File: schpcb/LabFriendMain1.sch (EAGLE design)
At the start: 299 parts, among them IC1 TPS62560, IC10 TPS62560, IC11 TPS62560, IC12 TPS62560, IC14 TPS72301, IC18 LM358D, IC19 LM358D, IC2 25px80, IC20 PCM3010, IC21 TS922, IC23 TS922, IC24 4052D, IC25 ADS1112, IC26 MT41J128M8, IC3 SI8462, IC4 FT232H, IC5 ADC08200, IC6 ADC08200, IC8 93LC56SM, IC9 74LVC8T245, Q1 12MHz, U2 6SLX9FTG256, X1 MINI-USB-32005-201

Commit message: current state
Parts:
- added C100, C102: 2n2, passive:CAPC0603
- added C101, C114, C98, C99: 330pF, passive:CAPC0603
- added C103, C113: 47uF, passive:CAPC1206
- added C115, C116, C145, C146, C147, C193, C197, C198, C96, C97: 100nF, passive:CAPC0402
- added C148, C150: (no value), passive:CAPC0402
- added C149: 100pF, teg2:C0603
- added C151, C152: 47pF, teg2:C0603
- added C153, C154: 100n, teg2:C0603
- added C155, C156, C160: 100nF, teg2:C0603
- added C157, C158, C159, C161: 100µF, rcl:CPOL-EUCT6032
- added C162, C173, C178, C181, C188, C189, C191, C196, C199: 1uF, passive:CAPC0603
- added C163, C174: 22pF, passive:CAPC0603
- added C164: 100uF, passive:CAPC0402
- added C165, C171, C177, C179, C180, C182, C183, C184, C185, C186, C187, C192, C194, C200: 10uF, passive:CAPC0603
- added C166: 470nF, passive:CAPC1206
- added C167: 470nF, passive:CAPC0402
- added C168, C169, C170, C175, C176: 10µF, passive:CAPC0603
- added C172, C190, C195: 10nF, passive:CAPC0603
- added D1, D2, D3, D4, D5, D6: SK14, diode:DIODE-DO214AC
- added IC13: AK4621, data-converters:AK4621
- added IC15: LME49721, linear:LM358D
- added IC16: NE5532, linear:LM358D
- added IC17: OPA2134, linear:LM358D
- added IC22: 4052D, 40xx:4052D
- added IC27: 74HCT132D, 74xx-eu:74HCT132D
- added IC28: TPS72301, seabed:TPS72301
- added IC29: (no value), seabed:TPS73001
- added IC30: LM8272, linear:LMV358MM
- added IC31: LMV358MM, linear:LMV358MM
- added L11: (no value), passive:INUDCTOR0603
- added Q2, Q3: FDN335N, transistor-small-signal:BSS123
- added R132, R133, R134: 1k5, passive:RESR0603
- added R135, R136, R137, R138: 3k, passive:RESR0603
- added R139, R140, R141, R142: 22R, teg2:R0603
- added R143, R144: 10k, passive:RESR0603
- added R145, R147, R148, R149, R181, R182, R189, R190, R191, R194, R196, R200, R58, R74: 4k7, passive:RESR0603
- added R146, R150: 220k, passive:RESR0603
- added R151: 4k7, teg2:R0603
- added R152: 100R, teg2:R0603
- added R153, R163, R164, R166, R167, R175, R176: (no value), passive:RESR0603
- added R154: 1M, passive:RESR0603
- added R155, R187, R188: 100k, passive:RESR0603
- added R156: 1k, passive:RESR0603
- added R157, R158: 10k, teg2:R0603
- added R159, R160: 1.54k, teg2:R0603
- added R161, R162: 150, teg2:R0603
- added R165, R168, R172, R173, R174, R177, R178, R179, R180, R183, R184, R185, R186, R192, R193: 0R1, passive:RESR0603
- added R169: 1M, passive:RESR0402
- added R170, R171: 820k, passive:RESR0603
- added R195: 1k3, passive:RESR0603
- added R197: 5k1, passive:RESR0603
- added R198: 68k, passive:RESR0603
- added R199: 15k, passive:RESR0603
- added R56, R57: 200, passive:RESR0603
- added T1: EFD15DCDCPM5P33EFD15, transformers:EFD15DCDCPM5P33EFD15
- C1, C2, C3, C78, C79, C80, C82, C88, C92, C93: device teg2:C0603 -> passive:CAPC0603
- C104, C105, C112: device teg2:C0603 -> passive:CAPC0402
- C106, C107, C108, C109, C110, C111, C118, C125, C13, C134, C137, C138, C14, C140, C141, C28, C32, C33, C58, C60, C61, C62, C63, C64, C65, C67, C68, C69, C76, C77: device rcl:C-EUC0402 -> passive:CAPC0402
- C11: device rcl:C-EUC1206 -> passive:CAPC1206
- C117, C126: value 10uF -> 100nF; device rcl:C-EUC0603K -> passive:CAPC0402
- C119, C29, C30, C31, C36, C37, C39, C40, C41, C42, C43, C44, C45, C46, C47, C48, C49, C50, C52, C53, C54, C55, C56, C74: device rcl:C-EUC0603K -> passive:CAPC0603
- C12, C57, C59, C66, C70: device rcl:C-EUC0603 -> passive:CAPC0603
- C120, C73: value 100nF -> 10uF; device rcl:C-EUC0402 -> passive:CAPC0603
- C121, C123: value 10uF -> 330pF; device rcl:C-EUC0603K -> passive:CAPC0603
- C122, C124: value 100nF -> 330pF; device rcl:C-EUC0402 -> passive:CAPC0603
- C127: value 10uF -> 10nF; device rcl:C-EUC0603K -> passive:CAPC0603
- C128: value 200pF -> 330pF; device rcl:C-EUC0603K -> passive:CAPC0603
- C129, C130, C131, C132, C133: value 200pF -> 47uF; device rcl:C-EUC0603K -> passive:CAPC1206
- C135, C136: value 10uF -> 47uF; device rcl:C-EUC0603K -> passive:CAPC1206; VOLTAGE (none) -> 10V
- C21, C23, C35: value 4u7 -> 100uF; device rcl:C-EUC0603K -> passive:CAPC1206
- C22, C25: value 4u7 -> 470nF; device rcl:C-EUC0603K -> passive:CAPC0402
- C24: value 4u7 -> 10uF; device rcl:C-EUC0603K -> passive:CAPC0603
- C26, C38: device rcl:C-EUC0603K -> passive:CAPC0402
- C34: value 470nF -> 10uF; device rcl:C-EUC0402 -> passive:CAPC0603
- C71: value 10uF -> 100uF; device rcl:C-EUC0603 -> passive:CAPC1206
- C72: value 100nF -> 470nF; device rcl:C-EUC0402 -> passive:CAPC0402
- C81: value 33pF -> 10uF; device teg2:C0603 -> passive:CAPC0603
- C83, C87: value 10µF -> 10nF; device teg2:C0603 -> passive:CAPC0603
- C84: value 33pF -> 1uF; device teg2:C0603 -> passive:CAPC0603
- C85: value 10µF -> 22pF; device teg2:C0603 -> passive:CAPC0603
- C86: value 10µF -> 10uF; device teg2:C0603 -> passive:CAPC0603
- C91, C95: device passive:CAPC0402 -> passive:CAPC0603
- IC11, IC12: value TPS62560 -> (none); device seabed:TPS62560 -> seabed:TPS73001
- IC18: value LM358D -> LM8272; device linear:LM358D -> linear:LMV358MM
- IC19: value LM358D -> LMV358MM; device linear:LM358D -> linear:LMV358MM
- IC20: value PCM3010 -> ISL54405IRTZ; device parts2004:PCM3010 -> switch_mux:ISL54405IRTZ
- IC21: value TS922 -> NE5532
- IC23: value TS922 -> LME49721
- IC24: value 4052D -> 74HC00D; device 40xx:4052D -> 74xx-eu:74HC00D
- L10, L8, L9: value 4.7uH -> (none); device rcl:L-USL3216C -> passive:INUDCTOR0603
- R10, R100, R101, R102, R103, R11, R12, R22, R23, R24, R25, R26, R27, R28, R29, R30, R31, R32, R33, R34, R35, R36, R37, R4, R5, R6, R79, R8, R88, R89, R9, R97, R98, R99: device teg2:R0603 -> passive:RESR0402
- R105, R94: value 47R -> 200; device teg2:R0603 -> passive:RESR0603
- R106: value 47R -> 1k5; device teg2:R0603 -> passive:RESR0603
- R107, R112, R14, R15, R16, R17, R18, R19, R20, R21, R38, R39, R40, R41, R42, R43, R44, R45, R46, R47, R52, R53, R65, R66, R75, R76, R77, R78, R93: device teg2:R0603 -> passive:RESR0603
- R48, R50: value 820k -> 0R1; device teg2:R0603 -> passive:RESR0603
- R49, R51: value 180k -> 0R1; device teg2:R0603 -> passive:RESR0603
- R54, R55: value RESR0603 -> (none)
- R61, R63: value 51k -> 68k; device teg2:R0603 -> passive:RESR0603
- R62, R64: value 22k -> 15k; device teg2:R0603 -> passive:RESR0603
- R83, R91: value 10M -> 4k7; device teg2:R0603 -> passive:RESR0603
- R84, R85: value 6k8 -> 4k7; device teg2:R0603 -> passive:RESR0603
- R86, R87: value 47R -> 600R
- R92: value 47R -> 4k7; device teg2:R0603 -> passive:RESR0603
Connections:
- removed net +5V/1: C3.2, C80.2, C83.2, C86.2, IC1.EN, IC1.VIN, IC10.EN, IC10.VIN, IC11.EN, IC11.VIN, IC12.EN, IC12.VIN
- removed net -2V2: C105.2, C137.1, C141.2, IC18P.V-, IC23P.V-, IC24P.VEE
- removed net ASEL1: IC24A.B
- removed net HPADSPICS: IC3.B5, U2B2.IO_L31P_GCLK31_D14_2
- new net +3.6VBR: C162.2, C3.2, C80.2, C84.2, IC1.EN, IC1.VIN, IC10.EN, IC10.VIN, IC11.EN, IC11.IN, IC12.EN, IC12.IN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
- new net +3.6VI: C94.2, IC7.EN, IC7.IN, R179.P$1
- new net +5.5V: C156.1, C157.+, D1.C, D2.C, R178.P$1
- new net +5.5VI: C173.2, IC29.EN, IC29.IN, R178.P$2
- new net -2.5VI: C93.1, IC14.OUT, R174.P$1, R52.P$2
- new net -2V5: C176.1, C198.2, R174.P$2
- new net -5.5V: C155.2, C158.-, D3.A, D4.A, R172.P$1
- new net 1V2REFAD0: C111.1, IC5.VRB, L10.2
- new net 1V2REFAD1: C108.1, IC6.VRB, L9.2
- new net 2V8REFAD0: C109.1, IC5.VRT, L11.2
- new net 2V8REFAD1: C106.1, IC6.VRT, L8.2
- new net AUADCINL: C132.1, IC17B.-IN, IC17B.OUT, R149.P$2
- new net AUADCINR: C130.1, IC17A.-IN, IC17A.OUT, R147.P$2
- new net AUBIAS: C133.2, C134.2, IC15A.-IN, IC15B.+IN, IC23A.+IN, IC23B.+IN, R143.P$1, R144.P$2
- new net AUPDN: IC13.PDN
- new net AU_CCLK: IC13.CCLK/CKS1
- new net AU_CDTI: IC13.CDTI/CKS0
- new net AU_CSN: IC13.CSN/DIF
- new net AU_OVFL: IC13.OVFL/DZFL
- new net AU_OVFR: IC13.OVFR/DZFR
- new net AVREFM: C192.1, R192.P$2
- new net CMPMEAS_+: IC20.L2, R153.P$1, R154.P$1, R155.P$1, R156.P$1, SV4.1
- new net CMPMEAS_-: IC20.R2, IC22A.Y
- new net CMPMEAS_A: IC22A.A
- new net CMPMEAS_B: IC22A.B
- new net CMPMEAS_EN: IC22A.INH
- new net CMPMEAS_O: IC22A.X, R152.P$2
- new net EXVOI: IC19B.OUT, R185.P$1, R75.P$1
- new net LAD13OO: U2B2.IO_L13N_D10_2
- new net LADVREF: C167.1, R169.P$2, U2B2.IO_L16N_VREF_2, U2B2.IO_L48N_RDWR_B_VREF_2
- new net LAVIOI: C188.2, IC19A.OUT, R186.P$1, R66.P$1
- new net N$111: C101.1, IC21A.-IN, R94.P$2
- new net N$125: C121.1, IC23B.-IN, R106.P$1, R135.P$2
- new net N$152: C122.1, IC15A.+IN, R134.P$1, R137.P$2
- new net N$154: C123.1, IC15B.-IN, R133.P$1, R136.P$2
- new net N$156: C124.1, IC23A.-IN, R132.P$1, R138.P$2
- new net N$158: C127.2, IC13.AINL+, R140.P$1
- new net N$160: C127.1, IC13.AINL-, R139.P$2
- new net N$161: C128.1, IC13.AINR-, R142.P$2
- new net N$166: C128.2, IC13.AINR+, R141.P$1
- new net N$167: C129.2, R135.P$1
- new net N$168: C130.2, R138.P$1
- new net N$169: C131.2, R136.P$1
- new net N$170: C132.2, R137.P$1
- new net N$171: C131.1, IC16B.OUT, R148.P$1
- new net N$172: IC17B.+IN, IC20.R, R150.P$2
- new net N$173: IC17A.+IN, IC20.L, R146.P$2
- new net N$174: C146.2, IC20.CAP_SS
- new net N$175: C129.1, IC16A.OUT, R145.P$1
- new net N$176: IC16A.-IN, R145.P$2, R147.P$1
- new net N$177: IC16B.-IN, R148.P$2, R149.P$1
- new net N$178: IC20.R1, R151.P$1
- new net N$179: IC22A.X0, IC22A.Y0, R153.P$2
- new net N$180: IC22A.X1, IC22A.Y1, R154.P$2
- new net N$181: IC22A.X2, IC22A.Y2, R155.P$2
- new net N$182: IC22A.X3, IC22A.Y3, R156.P$2
- new net N$183: C148.2, C150.1, IC22P.GND
- new net N$184: IC27A.I0, IC27A.I1, R157.P$1
- new net N$185: IC24B.I0, IC24B.I1, IC27A.O
- new net N$186: C149.1, R157.P$2, R158.P$1
- new net N$187: C149.2, IC24A.I0, IC24A.I1, IC24B.O
- new net N$188: IC24A.O, IC27B.I0, IC27B.I1, IC27D.I0, R158.P$2, R160.P$1
- new net N$189: C151.2, IC27D.I1, R160.P$2
- new net N$190: IC27B.O, IC27C.I0, R159.P$1
- new net N$191: C152.2, IC27C.I1, R159.P$2
- new net N$192: IC24C.I0, IC24C.I1, IC27C.O
- new net N$193: IC24D.I0, IC24D.I1, IC27D.O
- new net N$194: IC24D.O, R161.P$1
- new net N$195: IC24C.O, R162.P$1
- new net N$196: Q3.G, R162.P$2
- new net N$197: D2.A, D3.C, T1.S1P
- new net N$198: D1.A, D4.C, T1.S1N
- new net N$199: Q2.D, T1.P1P
- new net N$200: Q2.G, R161.P$2
- new net N$201: Q3.D, T1.P1N
- new net N$202: D5.A, T1.S2P
- new net N$203: D6.A, T1.S2N
- new net N$204: R195.P$2, R197.P$1
- new net N$205: R43.P$1, U2B0.IO_L33P_0
- new net N$206: C81.2, C85.2, IC11.OUT, R163.P$2, R165.P$1
- new net N$207: C85.1, IC11.FB, R163.P$1, R164.P$2
- new net N$208: C163.2, C86.2, IC12.OUT, R166.P$2, R168.P$1
- new net N$209: C163.1, IC12.FB, R166.P$1, R167.P$2
- new net N$210: R169.P$1, U2B2.IO_L64N_D9_2
- new net N$211: C169.1, IC28.OUT, R170.P$2, R173.P$1
- new net N$212: IC28.FB, R170.P$1, R171.P$2
- new net N$213: C190.1, IC30A.OUT, R189.P$1, R192.P$1
- new net N$214: C172.2, IC29.NR
- new net N$215: C171.2, C174.2, IC29.OUT, R175.P$2, R177.P$1
- new net N$216: C174.1, IC29.FB, R175.P$1, R176.P$2
- new net N$217: C190.2, IC30A.-IN, R189.P$2
- new net N$218: C195.1, IC30B.OUT, R191.P$2, R193.P$1, R194.P$1
- new net N$219: C195.2, IC30B.-IN, R194.P$2
- new net N$220: C196.1, IC30B.+IN, R196.P$1, R197.P$2
- new net N$221: C199.1, IC31B.-IN, R198.P$2, R199.P$1
- new net N$223: C200.1, R199.P$2, R200.P$1
- new net N$23: C191.1, IC30A.+IN, R190.P$2, R191.P$1
- new net N$83: C135.2, R58.P$1
- new net N$88: C136.2, R74.P$1
- new net OFFSETCH0I: C178.1, IC18A.OUT, R183.P$1, R61.P$1
- new net OFFSETCH1I: C181.2, IC18B.OUT, R184.P$1, R63.P$1
- new net PWMEXVO: R188.P$2
- new net PWMLA: R200.P$2
- new net PWMLAVIO: R187.P$2
- new net PWMOFFS0: R181.P$2
- new net PWMOFFS1: R182.P$2
- net +3.6V: now also C160.1, C161.+, D5.C, D6.C, R179.P$2, R48.P$1; no longer C94.2, IC7.EN, IC7.IN
- net +3V3: now also C116.1, C117.1, C147.2, C164.2, C165.2, C166.2, IC13.DVDD, IC13.TVDD, R165.P$2, U2B0.IO_L1N_VREF_0, U2B0.IO_L2P_0, U2B0.IO_L3N_0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; no longer C125.1, C21.1, C81.2, IC20.DEMP0, IC20.FMT0, IC20.FMT1, IC20.PDOWN/, L8.2, R48.P$2
- net +5V: now also C104.2, C115.2, C119.2, C125.1, C126.1, C138.1, C141.1, C145.1, C148.1, C170.2, C96.1, IC13.AVDD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; no longer C123.1, C124.1, C134.1, C140.1, IC20.VCC1, IC20.VCC2, IC24P.VCC
- net +UB: now also C153.2, C154.2, C159.+, IC24P.VCC, IC27P.VCC, R51.P$2, T1.P1M; no longer C74.1, L6.1
- net -5V: now also C105.2, C137.1, C140.1, C150.2, C175.1, C97.1, IC16P.V-, IC17P.V-, IC18P.V-, IC21P.V-, IC22P.VEE, R173.P$2; no longer C93.1, IC14.OUT, R52.P$2
- net 1V2REF: now also C194.1, IC31B.+IN, L10.1, L9.1, R193.P$2; no longer C108.1, C111.1, IC24A.X2, IC24A.Y2, IC5.VRB, IC6.VRB
- net 2V8REF: now also C177.2, C193.2, IC30P.V+, L11.1, L8.1, R180.P$1, R190.P$1, R195.P$1; no longer C106.1, C109.1, IC5.VRT, IC6.VRT
- net 3V3A: now also C197.2, R168.P$2; no longer C104.2, C138.2, C87.2, IC18P.V+, IC23P.V+, L10.2
- net ADA0: now also U2B1.IO_L34N_A12_M1BA2_1; no longer U2B1.IO_L32N_A16_M1A9_1
- net ADA1: now also U2B1.IO_L34P_A13_M1WE_1; no longer U2B1.IO_L32P_A17_M1A8_1
- net ADA4: now also U2B1.IO_L33N_A14_M1A4_1; no longer U2B1.IO_L30N_A20_M1A11_1
- net ADA5: now also U2B1.IO_L33P_A15_M1A10_1; no longer U2B1.IO_L30P_A21_M1RESET_1
- net ADAC: now also U2B1.IO_L35P_A11_M1A7_1; no longer U2B1.IO_L33N_A14_M1A4_1
- net ADAP: now also U2B1.IO_L35N_A10_M1A2_1; no longer U2B1.IO_L33P_A15_M1A10_1
- net ADB0: now also U2B1.IO_L41N_GCLK8_M1CASN_1; no longer U2B1.IO_L38P_A5_M1CLK_1
- net ADB1: now also U2B1.IO_L44N_A2_M1DQ7_1; no longer U2B1.IO_L37N_A6_M1A1_1
- net ADB2: now also U2B1.IO_L44P_A3_M1DQ6_1; no longer U2B1.IO_L37P_A7_M1A0_1
- net ADB3: now also U2B1.IO_L43N_GCLK4_M1DQ5_1; no longer U2B1.IO_L36N_A8_M1BA1_1
- net ADB4: now also U2B1.IO_L37N_A6_M1A1_1; no longer U2B1.IO_L36P_A9_M1BA0_1
- net ADB5: now also U2B1.IO_L37P_A7_M1A0_1; no longer U2B1.IO_L35N_A10_M1A2_1
- net ADB6: now also U2B1.IO_L36N_A8_M1BA1_1; no longer U2B1.IO_L35P_A11_M1A7_1
- net ADB7: now also U2B1.IO_L32N_A16_M1A9_1; no longer U2B1.IO_L34N_A12_M1BA2_1
- net ADBC: now also U2B1.IO_L47N_LDC_M1DQ1_1; no longer U2B1.IO_L34P_A13_M1WE_1
- net AINL: no longer R92.P$2
- net AINR: now also R151.P$2; no longer R106.P$2, R93.P$2
- net ASEL0: no longer IC24A.A
- net EXVO: now also C184.1, R185.P$2; no longer IC19B.OUT, R75.P$1
- net GND: now also C114.1, C115.1, C116.2, C118.1, C119.1, C120.1, C126.2, C133.1, C134.1, C138.2, C141.2, C145.2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; no longer C118.2, C119.2, C120.2, C121.2, C122.2, C123.2, C124.2, C128.2, C129.2, C130.2, C131.2, C132.2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
- net GNDIO: now also C151.1, C152.1, C153.1, C154.1, C159.-, IC24P.GND, IC27P.GND, Q2.S, Q3.S
- net I2SBCK: now also IC13.BICK; no longer IC20.BCK, U2B2.IO_L64P_D8_2
- net I2SDATAIN: now also IC13.SDTI; no longer IC20.DIN
- net I2SLRCK: now also IC13.LRCK; no longer IC20.LRCK, U2B2.IO_L64N_D9_2
- net I2SSCLK: now also IC13.MCLK; no longer IC20.SCKI
- net LAD0: now also U2B2.IO_L23N_2
- net LAD1: now also U2B2.IO_L31P_GCLK31_D14_2
- net LAD10: now also U2B2.IO_L47P_2; no longer U2B1.IO_L39P_M1A3_1
- net LAD11: now also U2B2.IO_L29N_GCLK2_2; no longer U2B1.IO_L38N_A4_M1CLKN_1
- net LAD13: now also U2B2.IO_L14N_D12_2; no longer U2B2.IO_L13N_D10_2
- net LAD2: now also U2B2.IO_L30N_GCLK0_USERCCLK_2
- net LAD3: now also U2B2.IO_L32N_GCLK28_2
- net LAD4: now also U2B2.IO_L32P_GCLK29_2
- net LAD5: now also U2B2.IO_L47N_2; no longer U2B1.IO_L41N_GCLK8_M1CASN_1
- net LAD6: now also U2B2.IO_L48P_D7_2; no longer U2B1.IO_L41P_GCLK9_IRDY1_M1RASN_1
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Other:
- note removed: "120k"
- note removed: "3.15V"
- note removed: "3.1V"
- note removed: "510k"
- note removed: "750k"
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
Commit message: Pre release checkin
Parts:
- added C201, C202, C203: 10nF, passive:CAPC0402
- added C204, C206, C207, C208, C209, C210, C218, C219, C220, C221, C225, C226, C227, C231, C232, C233, C234, C235, C243, C244, C245, C246, C250, C251, C252, C255, C256: 100nF, passive:CAPC0402
- added C205, C230: 10uF, passive:CAPC0603
- added C211, C236: 100nF, passive:CAPC0603
- added C212, C214, C217, C222, C223, C237, C239, C242, C247, C248: 12pF, passive:CAPC0603
- added C213, C216, C238, C241: 6/30, rcl:C-TRIMMTZBX4
- added C215, C240: 220pF, passive:CAPC0603
- added C224, C249: 100uF, passive:CAPC1206
- added C228, C229, C253, C254: 1pF, passive:CAPC0603
- added IC32: ADS1118IDGSR, data-converters:ADS1118IDGSR
- added IC33, IC38: ADA4853-3RU, teg4:ADA4853-3RU
- added IC34, IC35, IC39, IC40: 4052D, 40xx:4052D
- added IC36, IC41: OPA2354, linear:AD8682RM
- added IC37, IC42, IC44: 74HC595D, 74xx-eu:74HC595D
- added IC43: LM321MF, linear:LM321MF
- added K1, K2, K3, K4: G6K-2F-Y, relay:G6K-2F-Y
- added L12, L14: 1uH, rcl:L-EUL3216C
- added R201: NC, passive:RESR0402
- added R202: 91k, passive:RESR0603
- added R203, R218, R219, R220, R254, R255, R256: 10k, passive:RESR0603
- added R204, R205: 27k, passive:RESR0603
- added R206, R207: 22k, passive:RESR0603
- added R208, R244: 200R, passive:RESR0603
- added R209, R245: 30R, passive:RESR0603
- added R210, R246: 20R, passive:RESR0603
- added R211, R214, R217, R237, R239, R247, R250, R253, R273, R275, R278, R279: 22R, passive:RESR0603
- added R212, R215, R216, R229, R230, R238, R248, R251, R252, R265, R266, R274, R300: 300R, passive:RESR0603
- added R213, R249, R277: 100R, passive:RESR0603
- added R221, R222, R257, R258: 30k, passive:RESR0603
- added R223, R224, R259, R260: 470k, passive:RESR0603
- added R225, R261: 51k, passive:RESR0603
- added R226, R262: 39k, passive:RESR0603
- added R227, R263: 910k, passive:RESR0603
- added R228, R264: 1k, passive:RESR0603
- added R231, R267: 7R5, passive:RESR0603
- added R232, R233, R234, R235, R236, R268, R269, R270, R271, R272: 10R, passive:RESR0603
- added R240, R276: 1R, passive:RESR0603
- added R241: 100R, passive:RESR0402
- added R242, R243: 47R, passive:RESR0603
- added R280: 1k, passive:RESR0402
- added R281: 2k2, passive:RESR0402
- added R282: 50R, passive:RESR0603
- added R283, R285, R292, R293, R294, R295, R296, R297, R298: 1k6, passive:RESR0603
- added R284, R286, R287, R288, R289, R290, R291: 820R, passive:RESR0603
- added R299: 39R, passive:RESR0603
- added SV5: 3x1 Pinheader, con-lstb:MA03-1
- added T10, T11, T14, T16, T2, T3, T4, T8: BC850, transistor:BC850
- added T12, T13, T15, T17, T5, T6, T7, T9: BC856ASMD, transistor-pnp:BC856ASMD
- added X2, X3: 31-5431-10RFX, connectors:227161-8
- C10, C139, C142, C143, C144, C15, C16, C17, C18, C20, C8, C9: device rcl:C-EUC0402 -> passive:CAPC0402
- C100, C101, C102, C114, C121, C122, C123, C124, C127, C98, C99: TYPE (none) -> NP0/C0G
- C12, C43, C44, C46, C48, C74: value 4.7uF -> 10uF
- C128: value 330pF -> 10nF; TYPE (none) -> NP0/C0G
- C129, C130, C131, C132, C133: VOLTAGE (none) -> 10V
- C148, C150: value (none) -> 100nF
- C149, C151, C152: device teg2:C0603 -> passive:CAPC0603
- C153, C154: value 100n -> 100nF; device teg2:C0603 -> passive:CAPC0402
- C155, C156, C160: device teg2:C0603 -> passive:CAPC0402
- C157, C158, C159, C161: value 100µF -> 100uF
- C163, C174, C85, C95: value 22pF -> 15pF
- C164: value 100uF -> 470nF
- C166: value 470nF -> 100uF
- C168, C169, C170, C175, C176, C2, C3, C79, C80, C82, C88, C92, C93: value 10µF -> 10uF
- C172, C190, C195, C36, C37, C39, C40, C41, C42, C45, C47, C49, C50, C52, C53, C54, C83, C87, C91: device passive:CAPC0603 -> passive:CAPC0402
- C51: device rcl:C-EUC0603K -> passive:CAPC0402
- IC1, IC10: value TPS62560 -> TPS62240DDC
- IC11, IC12, IC29, IC7: value (none) -> TPS73001DBVR
- IC22: value 4052D -> 74HC4052D
- IC25: value ADS1112 -> INA331IDGK; device teg4:ADS1112 -> amplifiers-and-linear:INA331IDGK
- L10, L11, L8, L9: value (none) -> 220nH
- L4, L5: device rcl:L-EUL3216C -> passive:INUDCTOR0603
- R1, R2: value 100 -> 100R; device teg2:R0603 -> passive:RESR0402
- R100, R101, R102, R103, R79, R97, R98, R99: value 47 -> 47R
- R104, R139, R140, R141, R142, R151, R157, R158, R59: device teg2:R0603 -> passive:RESR0603
- R105, R56, R57, R94: value 200 -> 200R
- R107, R46, R47: value 360 -> 360k
- R108, R109, R110, R111: value 6k8 -> 4k7; device teg2:R0603 -> passive:RESR0402
- R112: value 360 -> 240k
- R116, R117, R118, R119, R120, R121, R122, R123: value 100 -> 100R
- R146, R150: value 220k -> 1M
- R152, R7, R90: device teg2:R0603 -> passive:RESR0402
- R153: value (none) -> 1M
- R154: value 1M -> 100k
- R155: value 100k -> 1k
- R156: value 1k -> 68R
- R159, R160: value 1.54k -> 1k5; device teg2:R0603 -> passive:RESR0603
- R161, R162: value 150 -> 150R; device teg2:R0603 -> passive:RESR0603
- R163, R166: value (none) -> 43k
- R164, R167: value (none) -> 30k
- R170: value 820k -> 75k
- R171: value 820k -> 22k
- R175: value (none) -> 75k
- R176: value (none) -> 24k
- R18: value 2k -> 2k2; device passive:RESR0603 -> passive:RESR0402
- R195: value 1k3 -> 910R
- R22, R23, R24, R25, R26, R27, R28, R29, R30, R31, R32, R33, R34, R35, R36, R37: value 51R -> 47R
- R3: value 1k -> 240R; device rcl:R-EU_R0603 -> passive:RESR0603
- R38, R39, R40, R41, R42, R43, R44, R45: value 47 -> 47R; device passive:RESR0603 -> passive:RESR0402
- R5: value 22R -> 47R
- R52: value 820k -> 43k
- R53: value 820k -> 39k
- R54: value (none) -> 36k
- R55: value (none) -> 27k
- R6: value 24k -> 4k7
- R60: value 4k7 -> NC; device teg2:R0603 -> passive:RESR0402
- R86: value 600R -> 100R; device teg2:R0603 -> passive:RESR0402
- R87: value 600R -> 68R; device teg2:R0603 -> passive:RESR0603
- SV1: value (none) -> 2x5 Pinheader
- SV2, SV3, SV4: value (none) -> 2x8 Pinheader
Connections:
- removed net -2V5: C176.1, C198.2, R174.P$2
- removed net GPSPICLK: U2B2.IO_L2P_CMPCLK_2
- removed net GPSPICS: U2B2.IO_L12P_D1_MISO2_2
- removed net GPSPIDATA: U2B2.IO_L2N_CMPMOSI_2
- removed net LAD13OO: U2B2.IO_L13N_D10_2
- removed net N$148: IC25.AIN3, R111.P$2
- removed net SCL: IC25.SCL, R59.P$2
- removed net SDA: IC25.SDA, R60.P$2, U2B2.IO_L30P_GCLK1_D13_2
- new net -2V5A: C176.1, C198.2, C207.1, C209.1, C219.1, C232.1, C234.1, C244.1, IC31P.V-, IC34P.VEE, IC35P.VEE, IC36P.V-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
- new net ATTRL+: IC37A.QB, R234.P$2
- new net ATTRL+B: IC42A.QB, R270.P$2
- new net ATTRL-: IC37A.QA, R236.P$1
- new net ATTRL-B: IC42A.QA, R272.P$1
- new net AUXIN: IC34A.X3, R275.P$2
- new net AUXINCH0: IC25.VOUT, IC39A.X3, R202.P$2
- new net AUXOUT: R239.P$2
- new net CMP_MEAS_SEL: IC20.SEL, U2B1.IO_L49N_M1DQ11_1
- new net DCRL+: IC37A.QD, R235.P$2
- new net DCRL+B: IC42A.QD, R271.P$2
- new net DCRL-: IC37A.QC, R233.P$1
- new net DCRL-B: IC42A.QC, R269.P$1
- new net DC_CS: IC32.!CS, U2B1.IO_L74N_DOUT_BUSY_1
- new net DC_DOUT: R280.P$1, R281.P$1, U2B1.IO_L52N_M1DQ15_1
- new net GMUXA: IC34A.A, IC37A.QE
- new net GMUXAB: IC39A.A, IC42A.QE
- new net GMUXB: IC34A.B, IC37A.QF
- new net GMUXBB: IC39A.B, IC42A.QF
- new net GMUXC: IC35A.A, IC37A.QG
- new net GMUXCB: IC40A.A, IC42A.QG
- new net GMUXD: IC35A.B, IC37A.QH
- new net GMUXDB: IC40A.B, IC42A.QH
- new net HFDAC: R282.P$2, SV4.11
- new net HFDAC_CLK: IC44A.SCK, U2B1.IO_L32P_A17_M1A8_1
- new net HFDAC_CS: IC44A.RCK, U2B1.IO_L41P_GCLK9_IRDY1_M1RASN_1
- new net HFDAC_DI: IC44A.SER, U2B1.IO_L53N_VREF_1
- new net N$222: IC20.AC/DC, R201.P$1
- new net N$224: IC20.DIR_SEL, R60.P$1
- new net N$225: IC25.RG, R202.P$1, R203.P$2
- new net N$226: IC25.VIN+, R204.P$2, R207.P$2
- new net N$227: IC25.VIN-, R205.P$2, R206.P$1
- new net N$228: R204.P$1, SV5.3
- new net N$229: R205.P$1, SV5.1
- new net N$230: IC33A.IN-, R208.P$1, R209.P$2
- new net N$231: IC33A.OUT, R208.P$2, R211.P$2
- new net N$232: R209.P$1, R210.P$2
- new net N$233: IC33B.IN-, R212.P$1, R213.P$2
- new net N$234: IC33C.IN-, R215.P$1, R216.P$2
- new net N$235: IC33C.OUT, R215.P$2, R217.P$2
- new net N$236: IC33A.IN+, IC34A.X0, IC35A.X2, IC35A.Y1, R220.P$2, R231.P$1
- new net N$237: IC33B.OUT, R212.P$2, R214.P$2
- new net N$238: IC35A.X3, IC35A.Y0, R211.P$1
- new net N$239: IC33C.IN+, IC35A.X, R219.P$2
- new net N$240: IC34A.X1, IC35A.X0, R214.P$1
- new net N$241: IC34A.X2, R217.P$1
- new net N$242: IC33B.IN+, IC35A.Y, R218.P$2
- new net N$243: C211.2, K12.P, R241.P$1
- new net N$244: C211.1, K12.O, K22.P
- new net N$245: R221.P$2, R223.P$1
- new net N$246: C212.2, C214.1, C228.1, R221.P$1, R222.P$2, R242.P$2
- new net N$247: R222.P$1, R224.P$2
- new net N$248: C214.2, C223.2, C228.2, K22.S, R223.P$2
- new net N$249: R225.P$2, R227.P$1
- new net N$250: R226.P$1, R228.P$2
- new net N$251: C217.2, C222.2, C229.2, K22.O, R227.P$2
- new net N$252: IC36A.-IN, R229.P$1, R230.P$2
- new net N$253: IC36A.OUT, R229.P$2, R231.P$2
- new net N$254: IC34A.X, IC36B.+IN
- new net N$255: C224.1, R232.P$1, T2.C, T3.C, T4.C, T8.C
- new net N$256: K11.-, T3.E, T6.E
- new net N$257: K11.+, T2.E, T5.E
- new net N$258: R235.P$1, T2.B, T5.B
- new net N$259: R233.P$2, T3.B, T6.B
- new net N$260: K21.+, T4.E, T7.E
- new net N$261: K21.-, T8.E, T9.E
- new net N$262: R234.P$1, T4.B, T7.B
- new net N$263: R236.P$2, T8.B, T9.B
- new net N$264: IC36B.OUT, R237.P$2, R238.P$2, R239.P$1
- new net N$265: IC36A.+IN, K23.P
- new net N$266: C216.E, C222.1
- new net N$267: C213.E, C223.1
- new net N$268: IC36B.-IN, R238.P$1
- new net N$269: C220.2, L12.1, R230.P$1
- new net N$270: C215.2, C217.1, C229.1, R225.P$1, R226.P$2, R243.P$2
- new net N$271: R240.P$2, X2.2
- new net N$272: R241.P$2, X2.1
- new net N$273: K23.S, R242.P$1
- new net N$274: K23.O, R243.P$1
- new net N$281: IC38A.IN-, R244.P$1, R245.P$2
- new net N$282: IC38A.OUT, R244.P$2, R247.P$2
- new net N$283: R245.P$1, R246.P$2
- new net N$284: IC38B.IN-, R248.P$1, R249.P$2
- new net N$285: IC38C.IN-, R251.P$1, R252.P$2
- new net N$286: IC38C.OUT, R251.P$2, R253.P$2
- new net N$287: IC38A.IN+, IC39A.X0, IC40A.X2, IC40A.Y1, R256.P$2, R267.P$1
- new net N$288: IC38B.OUT, R248.P$2, R250.P$2
- new net N$289: IC40A.X3, IC40A.Y0, R247.P$1
- new net N$290: IC38C.IN+, IC40A.X, R255.P$2
- new net N$291: IC39A.X1, IC40A.X0, R250.P$1
- new net N$292: IC39A.X2, R253.P$1
- new net N$293: IC38B.IN+, IC40A.Y, R254.P$2
- new net N$294: C236.2, K32.P, R277.P$1
- new net N$295: C236.1, K32.O, K42.P
- new net N$296: R257.P$2, R259.P$1
- new net N$297: C237.2, C239.1, C253.1, R257.P$1, R258.P$2, R278.P$2
- new net N$298: R258.P$1, R260.P$2
- new net N$299: C239.2, C248.2, C253.2, K42.S, R259.P$2
- new net N$300: R261.P$2, R263.P$1
- new net N$301: R262.P$1, R264.P$2
- new net N$302: C242.2, C247.2, C254.2, K42.O, R263.P$2
- new net N$303: IC41A.-IN, R265.P$1, R266.P$2
- new net N$304: IC41A.OUT, R265.P$2, R267.P$2
- new net N$305: IC39A.X, IC41B.+IN
- new net N$306: C249.1, R268.P$1, T10.C, T11.C, T14.C, T16.C
- new net N$307: K31.-, T11.E, T13.E
- new net N$308: K31.+, T10.E, T12.E
- new net N$309: R271.P$1, T10.B, T12.B
- new net N$310: R269.P$2, T11.B, T13.B
- new net N$311: K41.+, T14.E, T15.E
- new net N$312: K41.-, T16.E, T17.E
- new net N$313: R270.P$1, T14.B, T15.B
- new net N$314: R272.P$2, T16.B, T17.B
- new net N$315: IC41B.OUT, R273.P$2, R274.P$2, R275.P$1
- new net N$316: IC41A.+IN, K43.P
- new net N$317: C241.E, C247.1
- new net N$318: C238.E, C248.1
- new net N$319: IC41B.-IN, R274.P$1
- new net N$320: C245.2, L14.1, R266.P$1
- new net N$321: C240.2, C242.1, C254.1, R261.P$1, R262.P$2, R279.P$2
- new net N$322: R276.P$2, X3.2
- new net N$323: R277.P$2, X3.1
- new net N$324: K43.S, R278.P$1
- new net N$325: K43.O, R279.P$1
- new net N$332: IC32.DOUT/!DRDY, R280.P$2
- new net N$333: R284.P$1, R285.P$1, R286.P$2
- new net N$334: R286.P$1, R287.P$2, R293.P$1
- new net N$335: R287.P$1, R288.P$2, R294.P$1
- new net N$336: R288.P$1, R289.P$2, R295.P$1
- new net N$337: R289.P$1, R290.P$2, R296.P$1
- new net N$338: R290.P$1, R291.P$2, R297.P$1
- new net N$339: R291.P$1, R292.P$2, R298.P$1
- new net N$340: R292.P$1, R299.P$2
- new net N$341: IC43.+IN, R283.P$2, R284.P$2
- new net N$342: IC44A.QA, R283.P$1
- new net N$343: IC44A.QB, R285.P$2
- new net N$344: IC44A.QC, R293.P$2
- new net N$345: IC44A.QD, R294.P$2
- new net N$346: IC44A.QE, R295.P$2
- new net N$347: IC44A.QF, R296.P$2
- new net N$348: IC44A.QG, R297.P$2
- new net N$349: IC44A.QH, R298.P$2
- new net N$350: IC43.-IN, R300.P$1
- new net N$351: IC43.OUT, R282.P$1, R300.P$2
- new net PULLUP1XA: R89.P$2, U2B2.IO_L1N_M0_CMPMISO_2
- new net SPICHAIN: IC37A.QH*, IC42A.SER
- new net SPICHAINB: IC42A.QH*
- new net SPICLK: IC37A.SCK, IC42A.SCK, U2B0.IO_L63N_SCP6_0
- new net SPICS: IC37A.RCK, IC42A.RCK, U2B0.IO_L65P_SCP3_0
- new net SPIDI: IC37A.SER, U2B0.IO_L65N_SCP2_0
- net +3V3: no longer R59.P$1, R60.P$1
- net +5V: now also C139.1, C204.2, C205.2, C206.2, C208.2, C210.2, C221.2, C230.2, C231.2, C233.2, C235.2, C246.2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
- net 3V3A: now also C218.2, C243.2, IC31P.V+, IC36P.V+, IC41P.V+; no longer C139.1, IC25.VDD
- net AINL: now also SV4.8; no longer SV4.10
- net AINR: now also SV4.7; no longer SV4.9
- net AUBIAS: now also IC15A.+IN; no longer IC15A.-IN
- net AUPDN: now also U2B1.IO_L49P_M1DQ10_1
- net AU_CCLK: now also IC32.SCLK, U2B1.IO_L51P_M1DQ12_1
- net AU_CDTI: now also IC32.DIN, U2B1.IO_L50N_M1UDQSN_1
- net AU_CSN: now also U2B1.IO_L51N_M1DQ13_1
- net AU_OVFL: now also U2B1.IO_L50P_M1UDQS_1
- net AU_OVFR: now also U2B1.IO_L46P_FCS_B_M1DQ2_1
- net AVREFM: now also C225.1, C226.1, C227.1, C250.1, C251.1, C252.1, IC25.REF, R203.P$1, R206.P$2, R207.P$1, R210.P$1, R213.P$1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
- net CMPMEAS_+: now also R59.P$2; no longer IC20.L2
- net CMPMEAS_A: now also U2B1.IO_L52P_M1DQ14_1
- net CMPMEAS_B: now also U2B1.IO_L74P_AWAKE_1
- net CMPMEAS_EN: now also U2B2.IO_L12P_D1_MISO2_2
- net EXVO: now also R111.P$1
- net EXVOI: now also C189.2
- net GND: now also C148.2, C150.1, C201.2, C202.2, C203.2, C204.1, C205.1, C206.1, C207.2, C208.1, C209.2, C210.1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; no longer IC25.A0, IC25.A1, IC25.GND, R3.1, SV4.11, SV4.7, SV4.8
- net I2SBCK: now also U2B1.IO_L45N_A0_M1LDQSN_1
- net I2SDATAIN: now also U2B1.IO_L46N_FOE_B_M1DQ3_1; no longer U2B2.IO_L62P_D5_2
- net I2SDATAOUT: now also U2B1.IO_L45P_A1_M1LDQS_1; no longer U2B2.IO_L62N_D6_2
- net I2SLRCK: now also U2B1.IO_L48P_HDC_M1DQ8_1
- net I2SSCLK: now also U2B1.IO_L48N_M1DQ9_1; no longer R89.P$2, U2B2.IO_L1N_M0_CMPMISO_2
- net N$117: now also C203.1, IC32.AIN0; no longer IC25.AIN0
- net N$142: now also C202.1, IC32.AIN1; no longer IC25.AIN1
- net N$144: now also C201.1, IC32.AIN2; no longer IC25.AIN2
- net N$149: now also R3.P$1; no longer R3.2
- net N$152: now also IC15A.-IN; no longer IC15A.+IN
- net N$162: now also SV4.15; no longer SV4.13
- net N$163: now also SV4.16; no longer SV4.14
- net N$164: now also IC32.AIN3, R111.P$2; no longer R110.P$1, SV4.15
- net N$165: now also R110.P$1, SV4.14; no longer R111.P$1, SV4.16
- net N$183: now also IC20.L2, R59.P$1; no longer C148.2, C150.1, IC22P.GND
- net OFFSETCH0: now also L14.2
- net OFFSETCH1: now also L12.2
- net OUTPUTCH0: now also R273.P$1
- net OUTPUTCH1: now also R237.P$1
- net PWMEXVO: now also U2B0.IO_L66P_SCP1_0
- net PWMLA: now also U2B1.IO_L1N_A24_VREF_1
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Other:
- note added: "1.2543V with 2V8REF=2.8583V"
- note added: "1.2V"
- note added: "1.5V"
- note added: "3.3V is 2.98V to reduce power consumption"
- note added: "OUTPUT AUXOUT AUXIN +5V -2.5VA +3VA"
- note added: "Resistor values giving 2.8583V"
- note added: "SPIDI SPICLK SPICS SPICHAIN"
- note added: "giving 1.604V range"

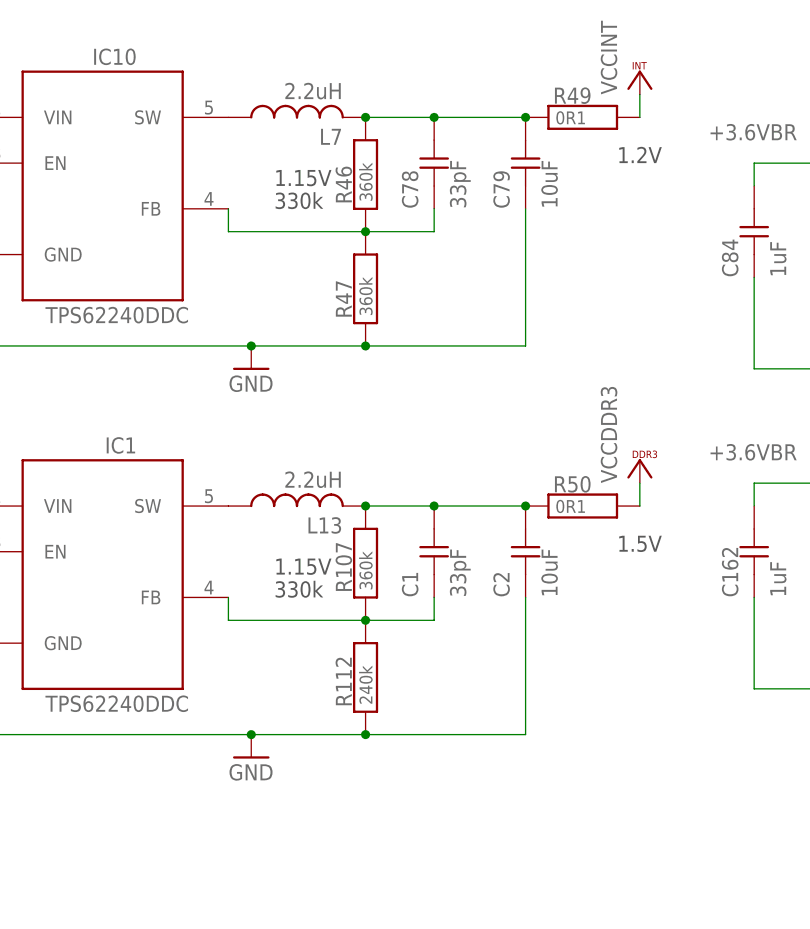
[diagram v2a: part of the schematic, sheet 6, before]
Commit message: Started adding chnge comments
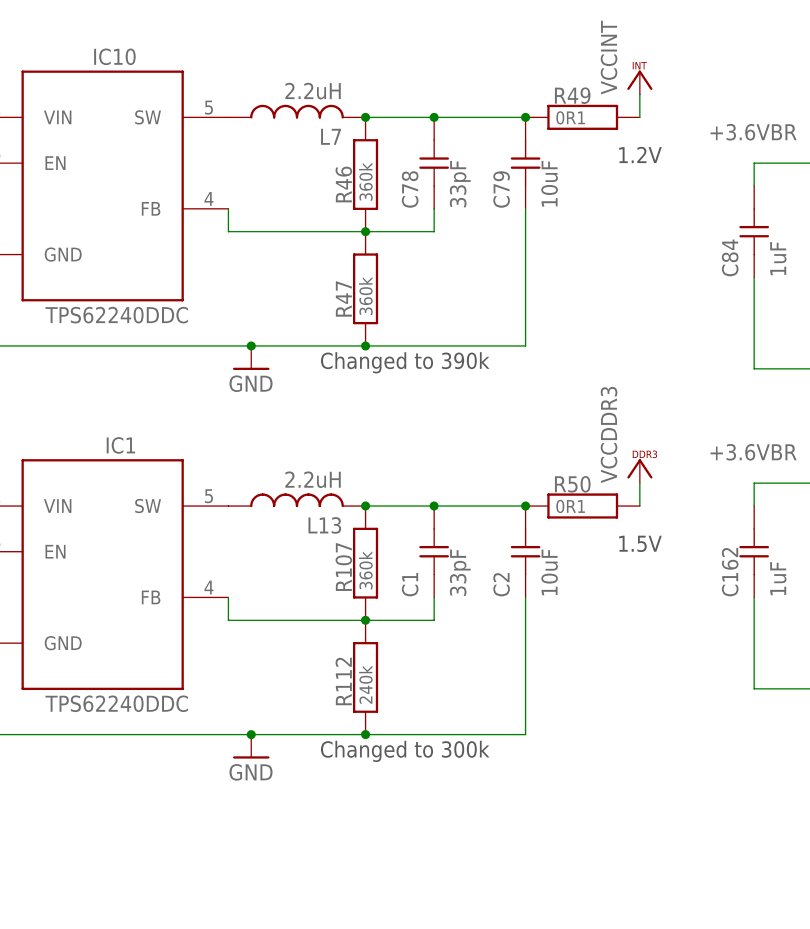
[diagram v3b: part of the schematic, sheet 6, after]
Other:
- note added: "Changed to 300k"
- note added: "Changed to 390k"
- note added: "Changed to 82p"
- note removed: "1.15V"
- note removed: "330k"
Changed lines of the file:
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@@
 <?xml version="1.0" encoding="utf-8"?>
 <!DOCTYPE eagle SYSTEM "eagle.dtd">
-<eagle version="7.3.0">
+<eagle version="7.2.0">
 <drawing>
 <settings>
@@
 <grid distance="0.1" unitdist="inch" unit="inch" style="lines" multiple="1" display="no" altdistance="0.01" altunitdist="inch" altunit="inch"/>
 <layers>
-<layer number="1" name="Top" color="4" fill="1" visible="yes" active="no"/>
-<layer number="2" name="Route2" color="1" fill="3" visible="yes" active="no"/>
-<layer number="3" name="Route3" color="6" fill="14" visible="yes" active="no"/>
-<layer number="14" name="Route14" color="1" fill="6" visible="yes" active="no"/>
-<layer number="15" name="Route15" color="4" fill="6" visible="yes" active="no"/>
-<layer number="16" name="Bottom" color="1" fill="1" visible="yes" active="no"/>
-<layer number="17" name="Pads" color="2" fill="1" visible="yes" active="no"/>
-<layer number="18" name="Vias" color="2" fill="1" visible="yes" active="no"/>
-<layer number="19" name="Unrouted" color="6" fill="1" visible="yes" active="no"/>
-<layer number="20" name="Dimension" color="15" fill="1" visible="yes" active="no"/>
-<layer number="21" name="tPlace" color="7" fill="1" visible="yes" active="no"/>
-<layer number="22" name="bPlace" color="7" fill="1" visible="yes" active="no"/>
-<layer number="23" name="tOrigins" color="15" fill="1" visible="yes" active="no"/>
-<layer number="24" name="bOrigins" color="15" fill="1" visible="yes" active="no"/>
-<layer number="25" name="tNames" color="7" fill="1" visible="yes" active="no"/>
-<layer number="26" name="bNames" color="7" fill="1" visible="yes" active="no"/>
-<layer number="27" name="tValues" color="7" fill="1" visible="yes" active="no"/>
-<layer number="28" name="bValues" color="7" fill="1" visible="yes" active="no"/>
+<layer number="1" name="Top" color="4" fill="1" visible="no" active="no"/>
+<layer number="2" name="Route2" color="1" fill="3" visible="no" active="no"/>
+<layer number="3" name="Route3" color="6" fill="14" visible="no" active="no"/>
+<layer number="14" name="Route14" color="1" fill="6" visible="no" active="no"/>
+<layer number="15" name="Route15" color="4" fill="6" visible="no" active="no"/>
+<layer number="16" name="Bottom" color="1" fill="1" visible="no" active="no"/>
+<layer number="17" name="Pads" color="2" fill="1" visible="no" active="no"/>
+<layer number="18" name="Vias" color="2" fill="1" visible="no" active="no"/>
+<layer number="19" name="Unrouted" color="6" fill="1" visible="no" active="no"/>
+<layer number="20" name="Dimension" color="15" fill="1" visible="no" active="no"/>
+<layer number="21" name="tPlace" color="7" fill="1" visible="no" active="no"/>
+<layer number="22" name="bPlace" color="7" fill="1" visible="no" active="no"/>
+<layer number="23" name="tOrigins" color="15" fill="1" visible="no" active="no"/>
+<layer number="24" name="bOrigins" color="15" fill="1" visible="no" active="no"/>
+<layer number="25" name="tNames" color="7" fill="1" visible="no" active="no"/>
+<layer number="26" name="bNames" color="7" fill="1" visible="no" active="no"/>
+<layer number="27" name="tValues" color="7" fill="1" visible="no" active="no"/>
+<layer number="28" name="bValues" color="7" fill="1" visible="no" active="no"/>
 <layer number="29" name="tStop" color="7" fill="3" visible="no" active="no"/>
 <layer number="30" name="bStop" color="7" fill="6" visible="no" active="no"/>
@@
 <layer number="35" name="tGlue" color="7" fill="4" visible="no" active="no"/>
 <layer number="36" name="bGlue" color="7" fill="5" visible="no" active="no"/>
-<layer number="37" name="tTest" color="7" fill="1" visible="yes" active="no"/>
-<layer number="38" name="bTest" color="7" fill="1" visible="yes" active="no"/>
+<layer number="37" name="tTest" color="7" fill="1" visible="no" active="no"/>
+<layer number="38" name="bTest" color="7" fill="1" visible="no" active="no"/>
 <layer number="39" name="tKeepout" color="4" fill="11" visible="no" active="no"/>
 <layer number="40" name="bKeepout" color="1" fill="11" visible="no" active="no"/>
@@
 <layer number="44" name="Drills" color="7" fill="1" visible="no" active="no"/>
 <layer number="45" name="Holes" color="7" fill="1" visible="no" active="no"/>
-<layer number="46" name="Milling" color="3" fill="1" visible="yes" active="no"/>
-<layer number="47" name="Measures" color="7" fill="1" visible="yes" active="no"/>
-<layer number="48" name="Document" color="7" fill="1" visible="yes" active="no"/>
-<layer number="49" name="Reference" color="7" fill="1" visible="yes" active="no"/>
-<layer number="50" name="dxf" color="7" fill="1" visible="yes" active="no"/>
-<layer number="51" name="tDocu" color="7" fill="1" visible="yes" active="no"/>
-<layer number="52" name="bDocu" color="7" fill="1" visible="yes" active="no"/>
-<layer number="53" name="tGND_GNDA" color="7" fill="1" visible="yes" active="no"/>
-<layer number="54" name="bGND_GNDA" color="7" fill="1" visible="yes" active="no"/>
+<layer number="46" name="Milling" color="3" fill="1" visible="no" active="no"/>
+<layer number="47" name="Measures" color="7" fill="1" visible="no" active="no"/>
+<layer number="48" name="Document" color="7" fill="1" visible="no" active="no"/>
+<layer number="49" name="Reference" color="7" fill="1" visible="no" active="no"/>
+<layer number="50" name="dxf" color="7" fill="1" visible="no" active="no"/>
+<layer number="51" name="tDocu" color="7" fill="1" visible="no" active="no"/>
+<layer number="52" name="bDocu" color="7" fill="1" visible="no" active="no"/>
+<layer number="53" name="tGND_GNDA" color="7" fill="1" visible="no" active="no"/>
+<layer number="54" name="bGND_GNDA" color="7" fill="1" visible="no" active="no"/>
 <layer number="90" name="Modules" color="5" fill="1" visible="yes" active="yes"/>
 <layer number="91" name="Nets" color="2" fill="1" visible="yes" active="yes"/>
@@
 <text x="160.02" y="-76.2" size="3.81" layer="96">Super Scope Pro +2</text>
 <text x="215.9" y="-73.66" size="2.1844" layer="96">PSU</text>
-<text x="99.06" y="58.42" size="1.778" layer="97">330k</text>
-<text x="99.06" y="60.96" size="1.778" layer="97">1.15V</text>
-<text x="99.06" y="15.24" size="1.778" layer="97">330k</text>
-<text x="99.06" y="17.78" size="1.778" layer="97">1.15V</text>
 <text x="238.76" y="22.86" size="1.778" layer="97" rot="R90">3.3V is 2.98V to reduce power consumption</text>
 <text x="137.16" y="63.5" size="1.778" layer="97">1.2V</text>
 <text x="137.16" y="20.32" size="1.778" layer="97">1.5V</text>
+<text x="104.14" y="-2.54" size="1.778" layer="97">Changed to 300k</text>
+<text x="104.14" y="40.64" size="1.778" layer="97">Changed to 390k</text>
 </plain>
 <instances>
@@
 <description>Isolated DCDC</description>
 <plain>
+<text x="12.7" y="50.8" size="1.778" layer="97">Changed to 82p</text>
 </plain>
 <instances>
